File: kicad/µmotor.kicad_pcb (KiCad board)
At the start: 4 copper layers, 20 x 20 mm, 60 parts, among them J101 CAN+PWR, J102 U, J103 V, J104 W, J105 U, J106 V, J107 W, J108 5V, J109 3V3, J110 IO, J111 GND, J201 A, J202 B, J203 6V, J204 GND, J501 SCL, J502 SDA, J503 3V3, J504 GND, J601 GND, J602 SWCLK, J603 SWDIO, J604 TX, Q301 FDMD82xx, Q302 FDMD82xx, Q303 FDMD82xx, U101 NCP4623HMX033TCG, U102 NCP4623HMX050TCG, U201 AS5045B, U301 DRV8323S, U401 TCAN330, U501 TMP006, U601 STM32L433C(B-C)Ux_u

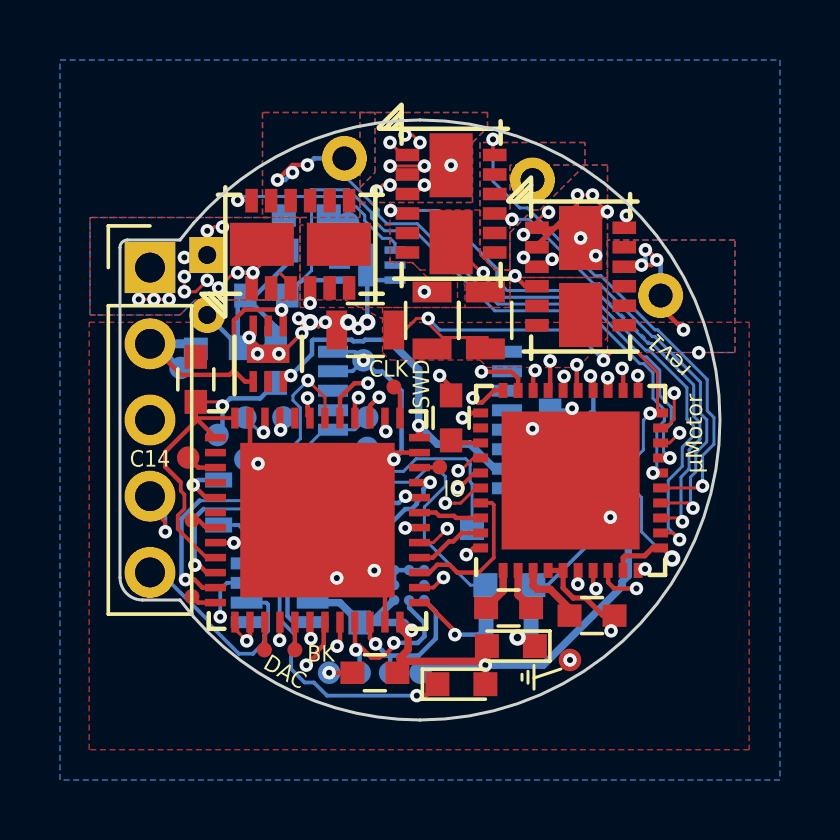
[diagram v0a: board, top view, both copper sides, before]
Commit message: add DRV8323 input cap, improve board outline
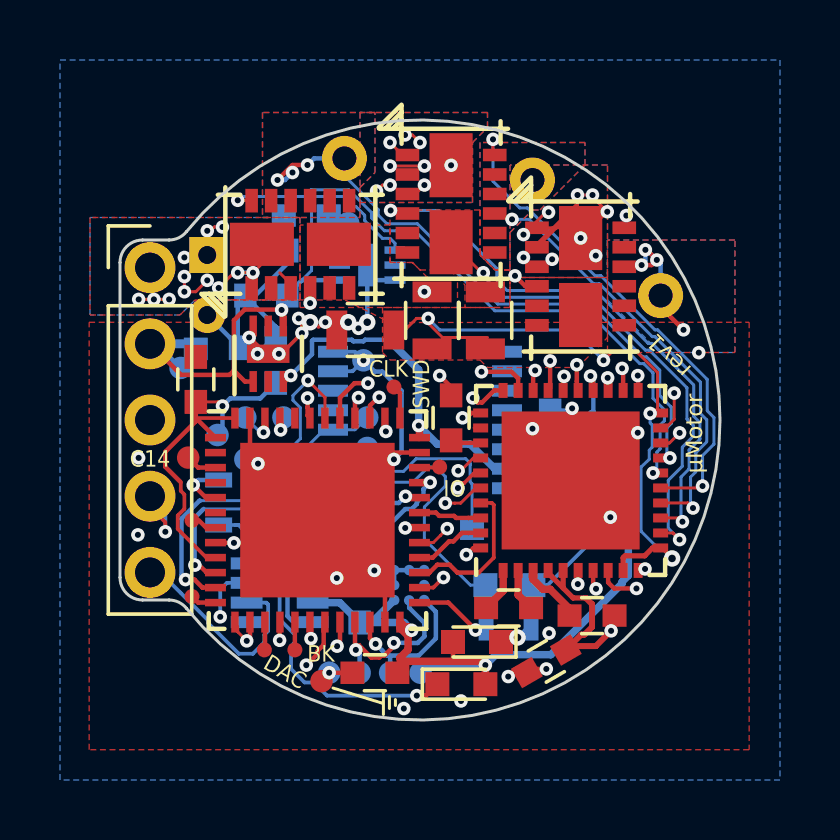
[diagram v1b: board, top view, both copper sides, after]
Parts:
- added C306: 100n 50V, Capacitors_SMD:C_0603, F.Cu at (164.2, 98.0)
- moved J601 8.31 mm to (156.7, 98.7)
- moved D601 1.14 mm to (161.9, 97.4)
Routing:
- net GND: track 75.0 -> 90.0 mm, vias 24 -> 31
- net +24V: track 54.3 -> 57.4 mm
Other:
- outline, holes or cut-outs redrawn

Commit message: layout: improvements
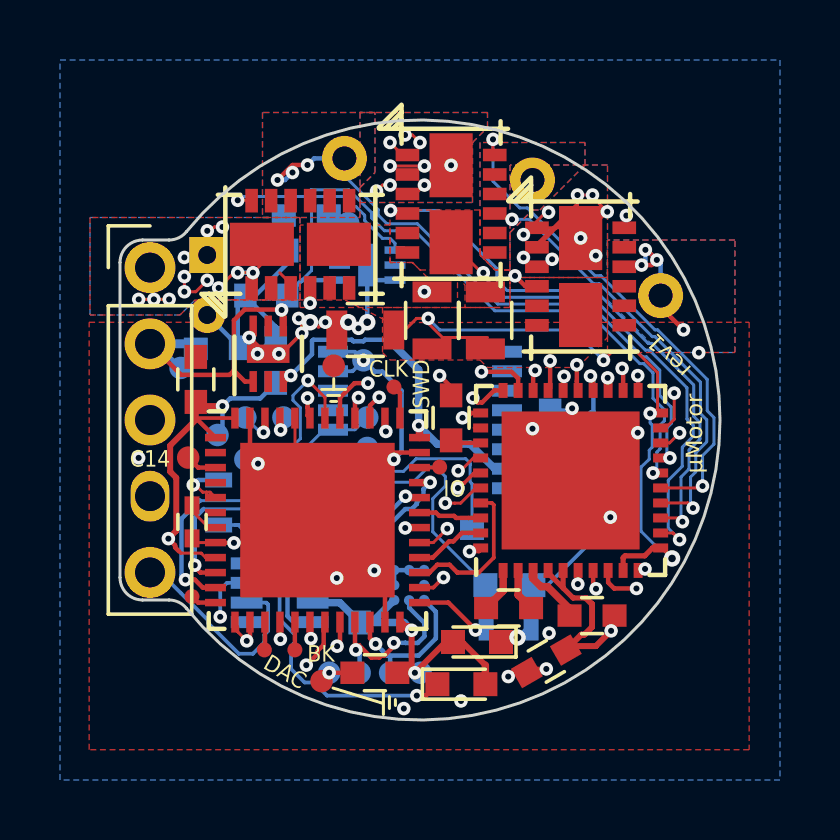
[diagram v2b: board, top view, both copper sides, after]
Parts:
- removed TP601: ~RST, Measurement_Point_Round-SMD-Pad_Smaller:Measurement_Point_Round-SMD-Pad_Smaller_0.5mm
- added C603: C, Capacitors_SMD:C_0402, F.Cu at (152.4, 93.4)
- added J112: GND, Measurement_Point_Round-SMD-Pad_Smaller:Measurement_Point_Round-SMD-Pad_Smaller_0.75mm, F.Cu at (156.7, 98.7)
- moved J601 10.5 mm to (157.1, 88.2)
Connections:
- U601 pad 44: (no net) -> GND
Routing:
- net GND: track 90.0 -> 85.9 mm, vias 31 -> 30
- net /CAN/CAN_H: track 8.94 -> 7.15 mm, vias 2 -> 1
- net Net-(D202-Pad1): track 9.21 -> 8.69 mm
- net +3V3: vias 6 -> 7
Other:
- board text added: "+3"

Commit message: increase via and track sizes
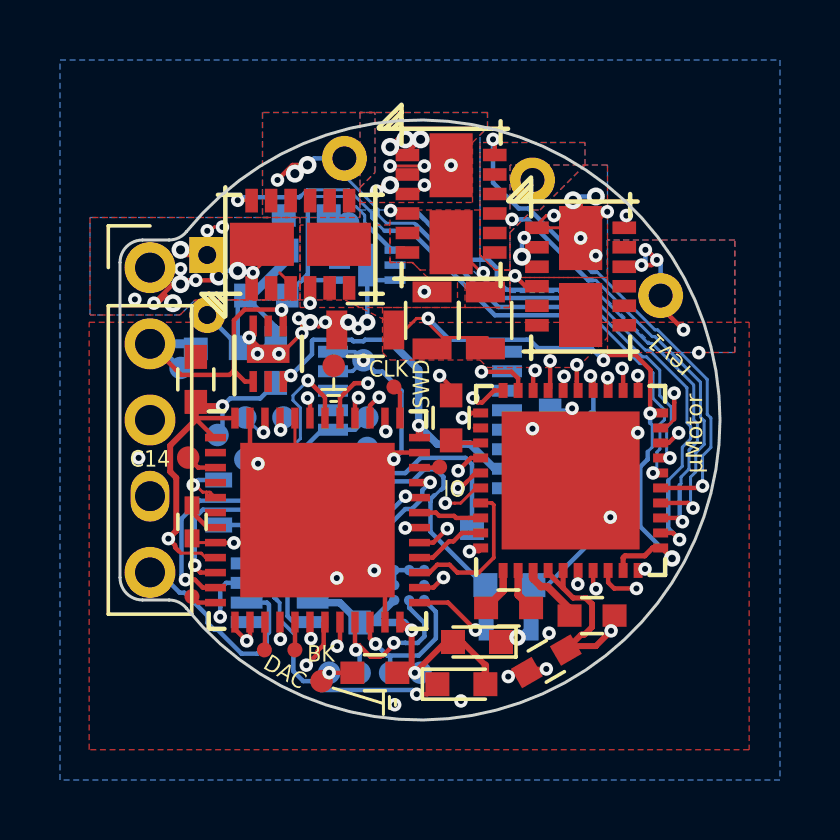
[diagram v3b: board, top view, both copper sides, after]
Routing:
- net +24V: track 57.4 -> 53.2 mm, vias 32 -> 31
- net /CAN/CAN_H: track 7.15 -> 8.03 mm
- net /CAN/CAN_L: track 7.20 -> 7.75 mm
